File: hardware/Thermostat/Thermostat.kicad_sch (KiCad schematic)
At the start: 44 parts, among them J1 MainConnectorr, J2 Screw_Terminal_01x02, J3 AVR-ISP-6, J4 Conn_01x03_Pin, J5 Conn_01x03_Pin, K1 G6E, K2 G6E, K3 G6E, K4 G6E, SW1_UP1 SW_Push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

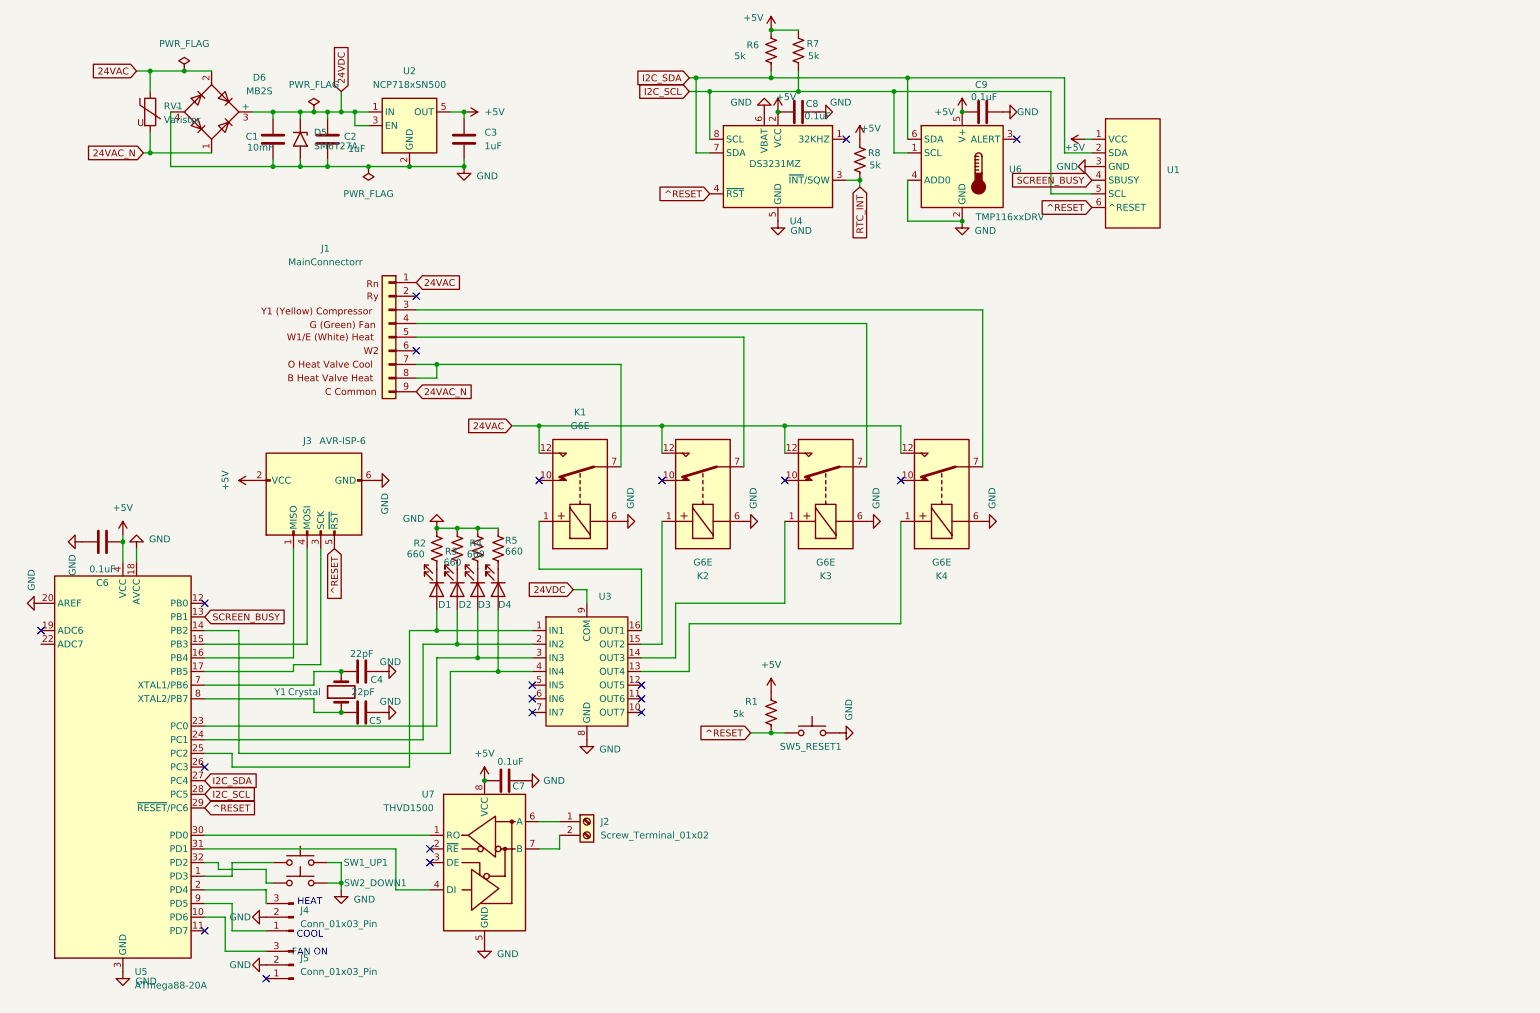
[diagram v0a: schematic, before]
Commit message: Project upgrade, add program button
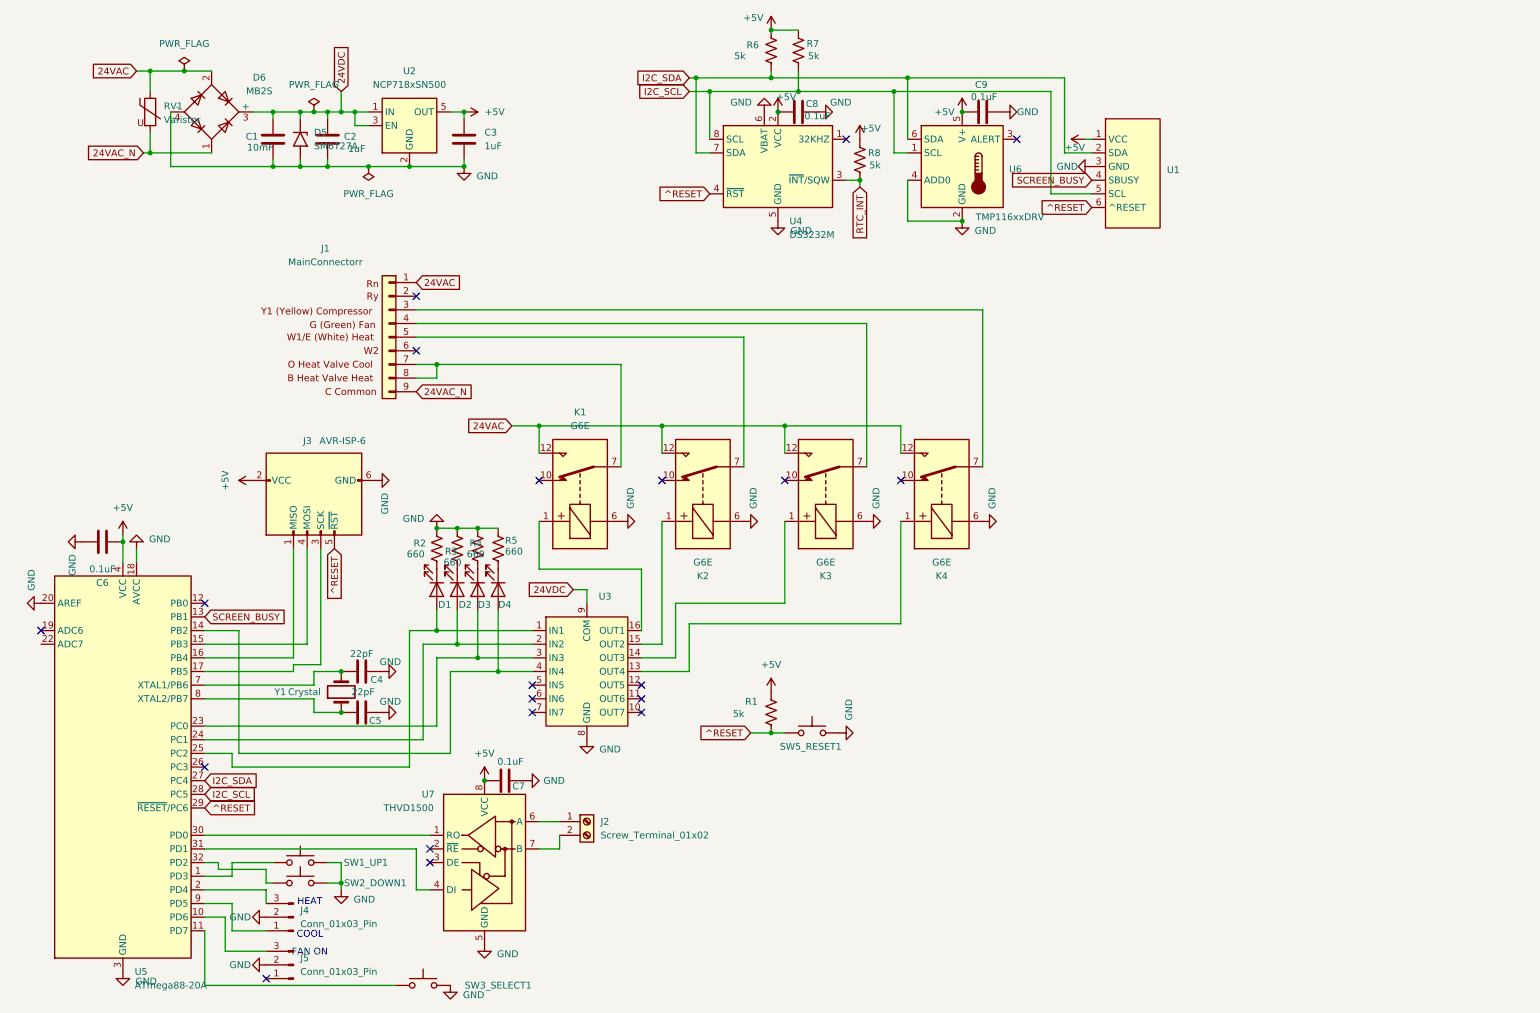
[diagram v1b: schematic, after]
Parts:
- removed U4: DS3231MZ, Package_SO:SOIC-8_3.9x4.9mm_P1.27mm, symbol Timer_RTC:DS3231MZ
- added SW3_SELECT1: SW_Push, Button_Switch_THT:SW_PUSH-12mm, symbol Switch:SW_Push
- added U4: DS3232M, Package_SO:SOIC-8_3.9x4.9mm_P1.27mm, symbol Timer_RTC:DS3232M
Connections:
- net +5V: now also U4.2 (VCC)
- net GND: now also SW3_SELECT1.2, U4.5 (GND), U4.6 (VBAT)
- net I2C_SCL: now also U4.8 (SCL)
- net I2C_SDA: now also U4.7 (SDA)
- net RTC_INT: now also U4.3 (~{INT}/SQW)
- net ^RESET: now also U4.4 (~{RST})
- net at U5.11 (PD7): now also SW3_SELECT1.1
- no-connect marks 21 -> 20
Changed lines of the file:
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@@
 	)
 	(junction
-		(at 160.02 31.75)
-		(diameter 0)
-		(color 0 0 0 0)
-	)
-	(junction
 		(at 194.31 31.75)
 		(diameter 0)
@@
 	)
 	(junction
+		(at 160.02 31.75)
+		(diameter 0)
+		(color 0 0 0 0)
+	)
+	(junction
 		(at 104.14 109.22)
 		(diameter 0)
@@
 	)
 	(no_connect
-		(at 53.34 184.15)
-	)
-	(no_connect
 		(at 134.62 140.97)
 	)
@@
 	(wire
 		(pts
+			(xy 53.34 194.31) (xy 88.9 194.31)
+		)
+		(stroke
+			(width 0)
+			(type default)
+		)
+	)
+	(wire
+		(pts
 			(xy 99.06 135.89) (xy 99.06 151.13)
 		)
@@
 	(wire
 		(pts
-			(xy 95.25 176.53) (xy 88.9 176.53)
+			(xy 95.25 176.53) (xy 92.71 176.53)
 		)
 		(stroke
@@
 	(wire
 		(pts
-			(xy 88.9 168.91) (xy 53.34 168.91)
+			(xy 92.71 168.91) (xy 53.34 168.91)
 		)
 		(stroke
@@
 	(wire
 		(pts
+			(xy 53.34 184.15) (xy 53.34 194.31)
+		)
+		(stroke
+			(width 0)
+			(type default)
+		)
+	)
+	(wire
+		(pts
 			(xy 41.91 39.37) (xy 43.18 39.37)
 		)
@@
 	(wire
 		(pts
-			(xy 88.9 176.53) (xy 88.9 168.91)
+			(xy 92.71 176.53) (xy 92.71 168.91)
 		)
 		(stroke
@@
 	)
 	(symbol
-		(lib_id "Timer_RTC:DS3231MZ")
-		(at 160.02 41.91 0)
-		(unit 1)
-		(exclude_from_sim no)
-		(in_bom yes)
-		(on_board yes)
-		(dnp no)
-		(property "Reference" "U4"
-			(at 162.2141 52.07 0)
-			(effects
-				(font
-					(size 1.27 1.27)
-				)
-				(justify left)
-			)
-		)
-		(property "Value" "DS3231MZ"
-			(at 154.686 41.402 0)
-			(effects
-				(font
-					(size 1.27 1.27)
-				)
-				(justify left)
-			)
-		)
-		(property "Footprint" "Package_SO:SOIC-8_3.9x4.9mm_P1.27mm"
-			(at 160.02 54.61 0)
-			(effects
-				(font
-					(size 1.27 1.27)
-				)
-				(hide yes)
-			)
-		)
-		(property "Datasheet" "http://datasheets.maximintegrated.com/en/ds/DS3231M.pdf"
-			(at 160.02 57.15 0)
-			(effects
-				(font
-					(size 1.27 1.27)
-				)
-				(hide yes)
-			)
-		)
-		(property "Description" "±5ppm, I2C Real-Time Clock SOIC-8"
-			(at 160.02 41.91 0)
-			(effects
-				(font
-					(size 1.27 1.27)
-				)
-				(hide yes)
-			)
-		)
-		(pin "8"
-		)
-		(pin "2"
-		)
-		(pin "1"
-		)
-		(pin "7"
-		)
-		(pin "4"
-		)
-		(pin "3"
-		)
-		(pin "6"
-		)
-		(pin "5"
-		)
-		(instances
-			(project ""
-				(path "/dae3c193-ffe6-4911-a810-cfe956c95f3b"
-					(reference "U4")
-					(unit 1)
-				)
-			)
-		)
-	)
-	(symbol
 		(lib_id "power:GND")
 		(at 167.64 31.75 90)
@@
 	)
 	(symbol
+		(lib_id "Switch:SW_Push")
+		(at 93.98 194.31 0)
+		(unit 1)
+		(exclude_from_sim no)
+		(in_bom yes)
+		(on_board yes)
+		(dnp no)
+		(property "Reference" "SW3_SELECT1"
+			(at 107.95 194.31 0)
+			(effects
+				(font
+					(size 1.27 1.27)
+				)
+			)
+		)
+		(property "Value" "SW_Push"
+			(at 93.98 189.23 0)
+			(effects
+				(font
+					(size 1.27 1.27)
+				)
+				(hide yes)
+			)
+		)
+		(property "Footprint" "Button_Switch_THT:SW_PUSH-12mm"
+			(at 93.98 189.23 0)
+			(effects
+				(font
+					(size 1.27 1.27)
+				)
+				(hide yes)
+			)
+		)
+		(property "Datasheet" "~"
+			(at 93.98 189.23 0)
+			(effects
+				(font
+					(size 1.27 1.27)
+				)
+				(hide yes)
+			)
+		)
+		(property "Description" "Push button switch, generic, two pins"
+			(at 93.98 194.31 0)
+			(effects
+				(font
+					(size 1.27 1.27)
+				)
+				(hide yes)
+			)
+		)
+		(pin "2"
+		)
+		(pin "1"
+		)
+		(instances
+			(project "Thermostat"
+				(path "/dae3c193-ffe6-4911-a810-cfe956c95f3b"
+					(reference "SW3_SELECT1")
+					(unit 1)
+				)
+			)
+		)
+	)
+	(symbol
 		(lib_id "power:GND")
 		(at 64.77 190.5 270)
@@
 	)
 	(symbol
+		(lib_id "power:GND")
+		(at 99.06 194.31 0)
+		(unit 1)
+		(exclude_from_sim no)
+		(in_bom yes)
+		(on_board yes)
+		(dnp no)
+		(property "Reference" "#PWR032"
+			(at 99.06 200.66 0)
+			(effects
+				(font
+					(size 1.27 1.27)
+				)
+				(hide yes)
+			)
+		)
+		(property "Value" "GND"
+			(at 103.378 196.088 0)
+			(effects
+				(font
+					(size 1.27 1.27)
+				)
+			)
+		)
+		(property "Footprint" ""
+			(at 99.06 194.31 0)
+			(effects
+				(font
+					(size 1.27 1.27)
+				)
+				(hide yes)
+			)
+		)
+		(property "Datasheet" ""
+			(at 99.06 194.31 0)
+			(effects
+				(font
+					(size 1.27 1.27)
+				)
+				(hide yes)
+			)
+		)
+		(property "Description" "Power symbol creates a global label with name \"GND\" , ground"
+			(at 99.06 194.31 0)
+			(effects
+				(font
+					(size 1.27 1.27)
+				)
+				(hide yes)
+			)
+		)
+		(pin "1"
+		)
+		(instances
+			(project "Thermostat"
+				(path "/dae3c193-ffe6-4911-a810-cfe956c95f3b"
+					(reference "#PWR032")
+					(unit 1)
+				)
+			)
+		)
+	)
+	(symbol
 		(lib_id "Device:LED")
 		(at 107.95 120.65 270)
@@
 					(unit 1)
 				)
+			)
+		)
+	)
+	(symbol
+		(lib_id "Timer_RTC:DS3232M")
+		(at 160.02 41.91 0)
+		(unit 1)
+		(exclude_from_sim no)
+		(in_bom yes)
+		(on_board yes)
+		(dnp no)
+		(fields_autoplaced yes)
+		(property "Reference" "U4"
+			(at 162.1633 52.07 0)
+			(effects
+				(font
+					(size 1.27 1.27)
+				)
+				(justify left)
+			)
+		)
+		(property "Value" "DS3232M"
+			(at 162.1633 54.61 0)
+			(effects
+				(font
+					(size 1.27 1.27)
+				)
+				(justify left)
+			)
+		)
+		(property "Footprint" "Package_SO:SOIC-8_3.9x4.9mm_P1.27mm"
+			(at 161.29 54.61 0)
+			(effects
+				(font
+					(size 1.27 1.27)
+				)
+				(hide yes)
+			)
+		)
+		(property "Datasheet" "http://datasheets.maximintegrated.com/en/ds/DS3232M.pdf"
+			(at 166.878 38.1 0)
+			(effects
+				(font
+					(size 1.27 1.27)
+				)
+				(hide yes)
+			)
+		)
+		(property "Description" "±5ppm, I2C Real-Time Clock with SRAM SOIC-8"
+			(at 160.02 41.91 0)
+			(effects
+				(font
+					(size 1.27 1.27)
+				)
+				(hide yes)
+			)
+		)
+		(pin "2"
+		)
+		(pin "6"
+		)
+		(pin "8"
+		)
+		(pin "1"
+		)
+		(pin "7"
+		)
+		(pin "3"
+		)
+		(pin "4"
+		)
+		(pin "5"
+		)
+		(instances
+			(project ""
+				(path "/dae3c193-ffe6-4911-a810-cfe956c95f3b"
+					(reference "U4")
+					(unit 1)
+				)

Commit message: Lots of work on JLCPCB parts
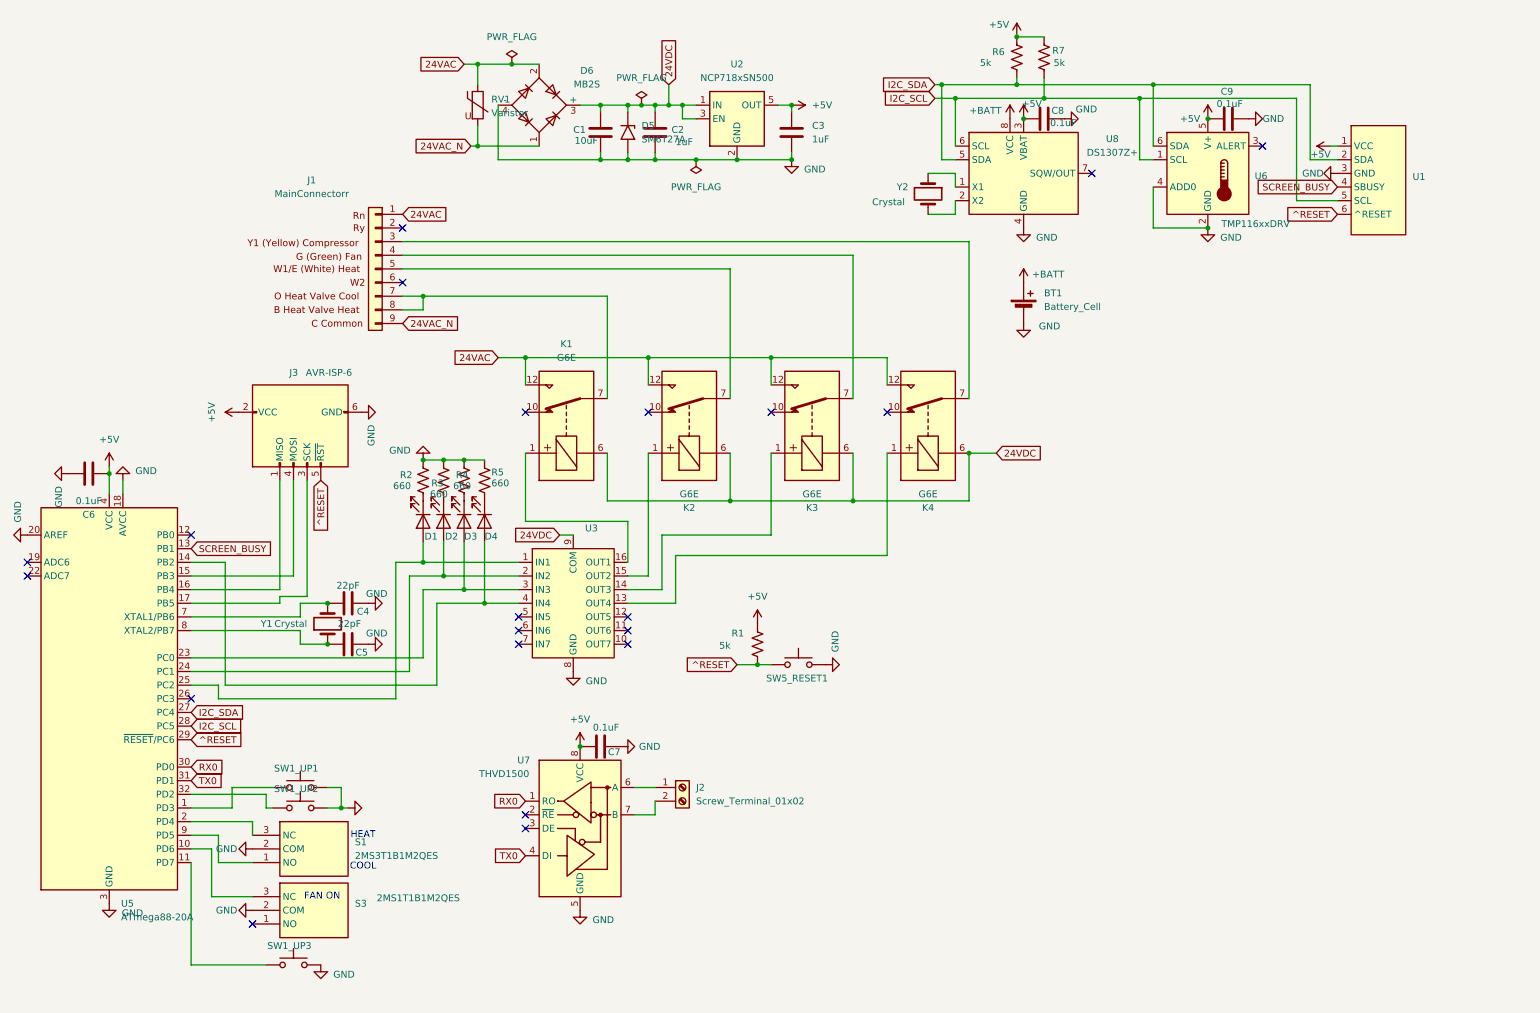
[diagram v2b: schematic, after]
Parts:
- removed J4, J5: Conn_01x03_Pin, Connector_PinSocket_2.54mm:PinSocket_1x03_P2.54mm_Vertical, symbol Connector:Conn_01x03_Pin
- removed R8: 5k, Resistor_SMD:R_0603_1608Metric, symbol Device:R_US
- removed SW2_DOWN1, SW3_SELECT1: SW_Push, Button_Switch_THT:SW_PUSH-12mm, symbol Switch:SW_Push
- removed U4: DS3232M, Package_SO:SOIC-8_3.9x4.9mm_P1.27mm, symbol Timer_RTC:DS3232M
- added BT1: Battery_Cell, Battery:BatteryHolder_Keystone_1058_1x2032, symbol Device:Battery_Cell
- added S1: 2MS3T1B1M2QES, ThermostatFootprints:2MS1T1B1M2QES, symbol ThermoSymbols:2MS3T1B1M2QES
- added S3: 2MS1T1B1M2QES, ThermostatFootprints:2MS1T1B1M2QES, symbol ThermoSymbols:2MS1T1B1M2QES
- added SW1_UP2, SW1_UP3: SW_Push, Button_Switch_THT:SW_PUSH-12mm, symbol Switch:SW_Push
- added U8: DS1307Z+, Package_SO:SOIC-8_3.9x4.9mm_P1.27mm, symbol Timer_RTC:DS1307Z+
- added Y2: Crystal, Crystal:Crystal_SMD_SeikoEpson_MA505-2Pin_12.7x5.1mm, symbol Device:Crystal
- C1: value 10mF -> 10uF
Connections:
- net +5V: now also U8.3 (VBAT)
- net 24VDC: now also K1.6, K2.6, K3.6, K4.6
- net GND: now also BT1.2 (-), S1.2 (COM), S3.2 (COM), SW1_UP2.2, SW1_UP3.2, U8.4 (GND); no longer K1.6, K2.6, K3.6, K4.6
- net I2C_SCL: now also U8.6 (SCL)
- net I2C_SDA: now also U8.5 (SDA)
- net at U5.32 (PD2): now also SW1_UP2.1
- net at U5.9 (PD5): now also S1.1 (NO)
- net at U5.2 (PD4): now also S1.3 (NC)
- net at U5.10 (PD6): now also S3.3 (NC)
- net at U5.11 (PD7): now also SW1_UP3.1
- net RX0: now reaches U5.30 (PD0), U7.1 (RO)
- net TX0: now reaches U5.31 (PD1), U7.4 (DI)
- new net: U8.1 (X1), Y2.1
- new net: U8.2 (X2), Y2.2
- new net +BATT: BT1.1 (+), U8.8 (VCC)
- no-connect marks 20 -> 21
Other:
- moved on the sheet: C1, C2, C3, C4, C5, C6, C7, C8, C9, D1, D2, D3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

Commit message: Much design work
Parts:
- removed U2: NCP718xSN500, Package_TO_SOT_SMD:SOT-23-5, symbol Regulator_Linear:NCP718xSN500
- removed Y2: Crystal, Crystal:Crystal_SMD_SeikoEpson_MA505-2Pin_12.7x5.1mm, symbol Device:Crystal
- added H1, H2, H3, H4: MountingHole, MountingHole:MountingHole_3mm, symbol Mechanical:MountingHole
- added U4: UA78M05QDCYRQ1, Package_TO_SOT_SMD:SOT-223-3_TabPin2, symbol Regulator_Linear:UA78M05QDCYRQ1
- added Y2: Crystal_GND23, ThermostatFootprints:MC-306_EPS, symbol Device:Crystal_GND23
- U1: value ~ -> GU112X16G-7003BL
- U6: footprint Package_SON:WSON-6-1EP_2x2mm_P0.65mm_EP1x1.6mm -> Package_SON:WSON-6-1EP_2x2mm_P0.65mm_EP1x1.6mm_ThermalVias
- renumbered SW1_UP2 to SW_DOWN1, SW1_UP3 to SW_SELECT1, SW1_UP1 to SW_UP1
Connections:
- net +5V: now also U4.3 (OUT)
- net 24VDC: now also U4.1 (IN)
- net GND: now also U4.2 (GND)
- net at U8.1 (X1): now also Y2.4
- net at U8.2 (X2): now also Y2.1
- no-connect marks 21 -> 23
